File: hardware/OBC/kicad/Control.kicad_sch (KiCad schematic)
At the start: 16 parts, among them J13 Conn_01x08_SocketMPU, J14 Conn_01x04_Socket, J15 Screw_Terminal_01x02, J16 Conn_01x02, J17 Conn_01x06_Socket, J18 Conn_01x02, J19 Conn_01x03, J20 Conn_01x02, J21 Conn_01x02, SW1 SW_SPDT, U1 25CSM04xxSN

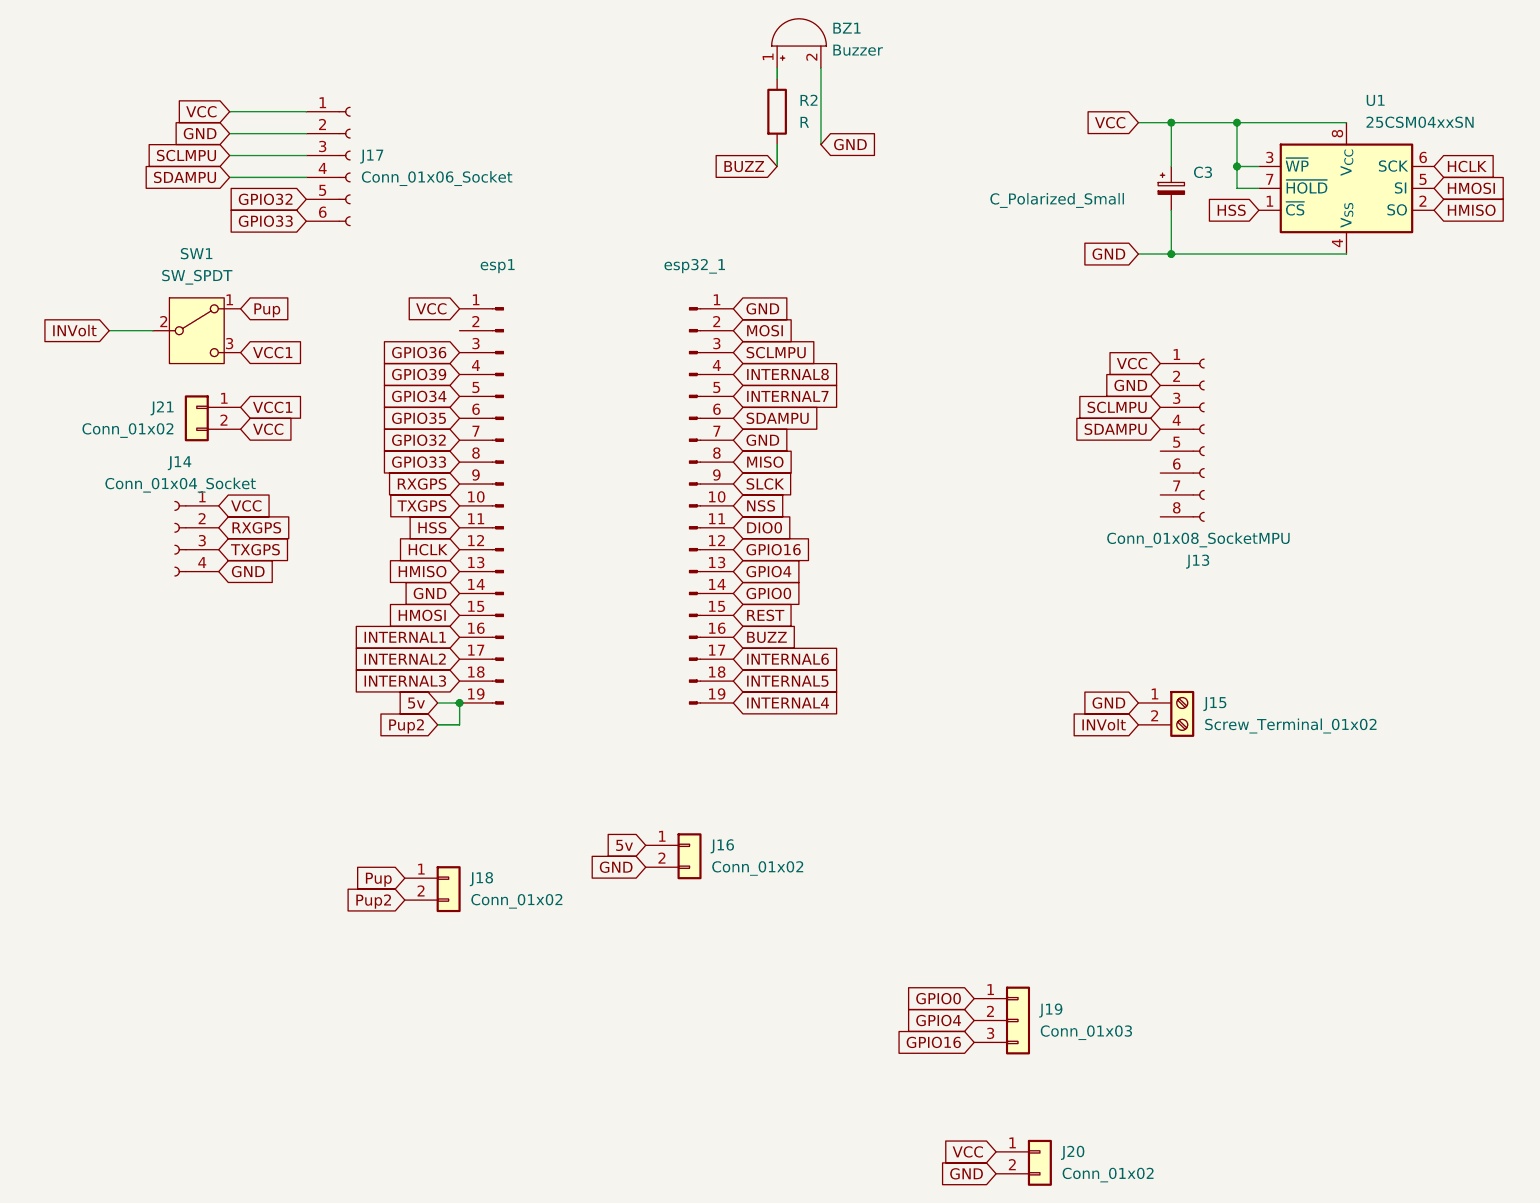
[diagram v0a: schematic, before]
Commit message: Add To-Do List in README.md general file, from specification of Servo-motor Connection, and add text in Hardware OBC schematic file.
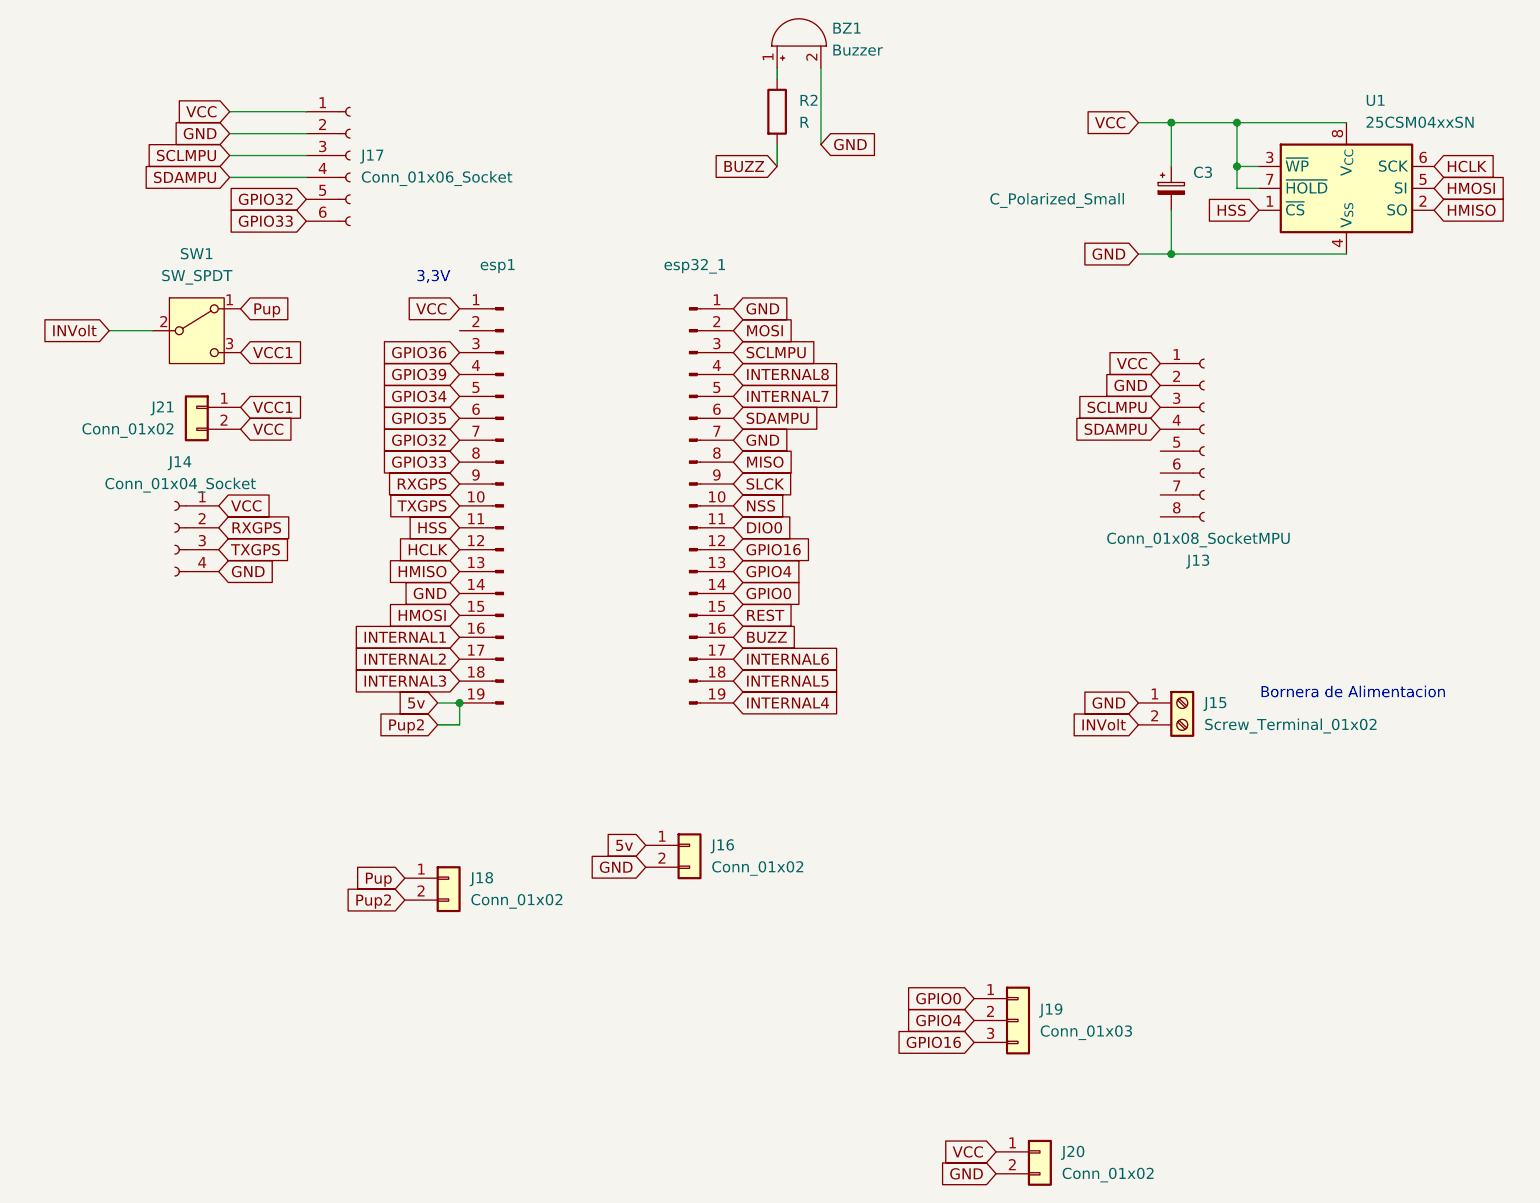
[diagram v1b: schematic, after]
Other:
- note added: "3,3V"
- note added: "Bornera de Alimentacion"
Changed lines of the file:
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@@
 	(generator_version "10.0")
 	(paper "A4")
+	(text "3,3V"
+		(exclude_from_sim no)
+		(at 71.882 59.944 0)
+		(effects
+			(font
+				(size 1.27 1.27)
+			)
+		)
+	)
+	(text "Bornera de Alimentacion"
+		(exclude_from_sim no)
+		(at 178.562 108.204 0)
+		(effects
+			(font
+				(size 1.27 1.27)
+			)
+		)
+	)
 	(junction
 		(at 74.93 109.22)
